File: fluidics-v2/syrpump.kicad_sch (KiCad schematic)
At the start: 7 parts, among them U5 MAX3221

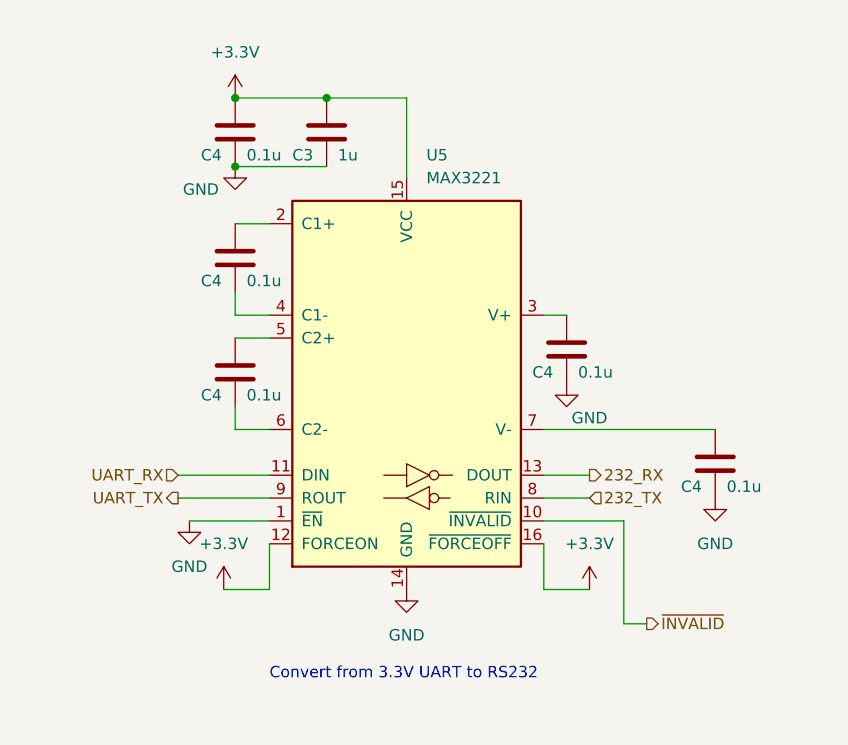
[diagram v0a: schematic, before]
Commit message: added footprints and mounting holes, cleaned up some sheets
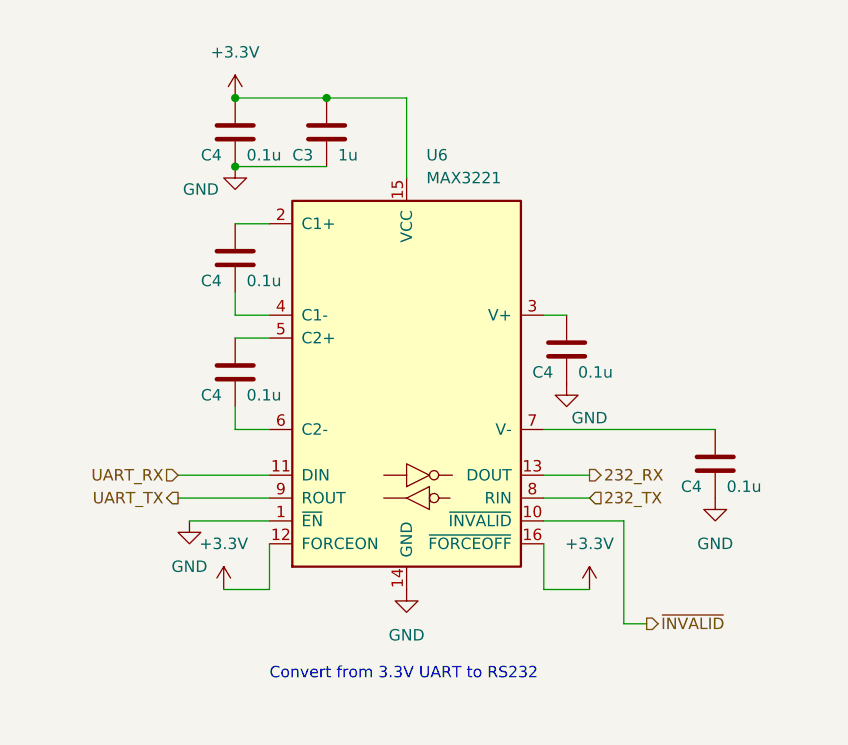
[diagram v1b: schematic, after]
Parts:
- renumbered U5 to U6
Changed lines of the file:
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@@
   (symbol (lib_id "power:+3.3V") (at 123.19 85.09 0) (unit 1)
     (in_bom yes) (on_board yes) (dnp no) (fields_autoplaced)
-    (property "Reference" "#PWR089" (at 123.19 88.9 0)
+    (property "Reference" "#PWR095" (at 123.19 88.9 0)
       (effects (font (size 1.27 1.27)) hide)
     )
@@
       (project "fluidics-v2"
         (path "/0ec91c42-8aad-437d-8c85-5e10f0e51fe0/40e657d1-9450-4917-aa0c-637ab5e93f67"
-          (reference "#PWR089") (unit 1)
+          (reference "#PWR095") (unit 1)
         )
       )
@@
   (symbol (lib_id "power:GND") (at 137.16 74.93 0) (unit 1)
     (in_bom yes) (on_board yes) (dnp no) (fields_autoplaced)
-    (property "Reference" "#PWR094" (at 137.16 81.28 0)
+    (property "Reference" "#PWR091" (at 137.16 81.28 0)
       (effects (font (size 1.27 1.27)) hide)
     )
@@
       (project "fluidics-v2"
         (path "/0ec91c42-8aad-437d-8c85-5e10f0e51fe0/40e657d1-9450-4917-aa0c-637ab5e93f67"
-          (reference "#PWR094") (unit 1)
+          (reference "#PWR091") (unit 1)
         )
       )
@@
         )
         (path "/0ec91c42-8aad-437d-8c85-5e10f0e51fe0/40e657d1-9450-4917-aa0c-637ab5e93f67"
-          (reference "C29") (unit 1)
+          (reference "C28") (unit 1)
         )
       )
@@
   (symbol (lib_id "power:GND") (at 83.82 38.1 0) (unit 1)
     (in_bom yes) (on_board yes) (dnp no)
-    (property "Reference" "#PWR092" (at 83.82 44.45 0)
+    (property "Reference" "#PWR089" (at 83.82 44.45 0)
       (effects (font (size 1.27 1.27)) hide)
     )
@@
       (project "fluidics-v2"
         (path "/0ec91c42-8aad-437d-8c85-5e10f0e51fe0/40e657d1-9450-4917-aa0c-637ab5e93f67"
-          (reference "#PWR092") (unit 1)
+          (reference "#PWR089") (unit 1)
         )
       )
@@
   (symbol (lib_id "power:+3.3V") (at 82.55 85.09 0) (unit 1)
     (in_bom yes) (on_board yes) (dnp no) (fields_autoplaced)
-    (property "Reference" "#PWR088" (at 82.55 88.9 0)
+    (property "Reference" "#PWR093" (at 82.55 88.9 0)
       (effects (font (size 1.27 1.27)) hide)
     )
@@
       (project "fluidics-v2"
         (path "/0ec91c42-8aad-437d-8c85-5e10f0e51fe0/40e657d1-9450-4917-aa0c-637ab5e93f67"
+          (reference "#PWR093") (unit 1)
+        )
+      )
+    )
+  )
+  (symbol (lib_id "power:GND") (at 120.65 62.23 0) (unit 1)
+    (in_bom yes) (on_board yes) (dnp no)
+    (property "Reference" "#PWR090" (at 120.65 68.58 0)
+      (effects (font (size 1.27 1.27)) hide)
+    )
+    (property "Value" "GND" (at 123.19 66.04 0)
+      (effects (font (size 1.27 1.27)))
+    )
+    (property "Footprint" "" (at 120.65 62.23 0)
+      (effects (font (size 1.27 1.27)) hide)
+    )
+    (property "Datasheet" "" (at 120.65 62.23 0)
+      (effects (font (size 1.27 1.27)) hide)
+    )
+    (pin "1")
+    (instances
+      (project "fluidics-v2"
+        (path "/0ec91c42-8aad-437d-8c85-5e10f0e51fe0/40e657d1-9450-4917-aa0c-637ab5e93f67"
+          (reference "#PWR090") (unit 1)
+        )
+      )
+    )
+  )
+  (symbol (lib_id "power:+3.3V") (at 83.82 30.48 0) (unit 1)
+    (in_bom yes) (on_board yes) (dnp no) (fields_autoplaced)
+    (property "Reference" "#PWR088" (at 83.82 34.29 0)
+      (effects (font (size 1.27 1.27)) hide)
+    )
+    (property "Value" "+3.3V" (at 83.82 25.4 0)
+      (effects (font (size 1.27 1.27)))
+    )
+    (property "Footprint" "" (at 83.82 30.48 0)
+      (effects (font (size 1.27 1.27)) hide)
+    )
+    (property "Datasheet" "" (at 83.82 30.48 0)
+      (effects (font (size 1.27 1.27)) hide)
+    )
+    (pin "1")
+    (instances
+      (project "fluidics-v2"
+        (path "/0ec91c42-8aad-437d-8c85-5e10f0e51fe0/40e657d1-9450-4917-aa0c-637ab5e93f67"
           (reference "#PWR088") (unit 1)
-        )
-      )
-    )
-  )
-  (symbol (lib_id "power:GND") (at 120.65 62.23 0) (unit 1)
-    (in_bom yes) (on_board yes) (dnp no)
-    (property "Reference" "#PWR093" (at 120.65 68.58 0)
-      (effects (font (size 1.27 1.27)) hide)
-    )
-    (property "Value" "GND" (at 123.19 66.04 0)
-      (effects (font (size 1.27 1.27)))
-    )
-    (property "Footprint" "" (at 120.65 62.23 0)
-      (effects (font (size 1.27 1.27)) hide)
-    )
-    (property "Datasheet" "" (at 120.65 62.23 0)
-      (effects (font (size 1.27 1.27)) hide)
-    )
-    (pin "1")
-    (instances
-      (project "fluidics-v2"
-        (path "/0ec91c42-8aad-437d-8c85-5e10f0e51fe0/40e657d1-9450-4917-aa0c-637ab5e93f67"
-          (reference "#PWR093") (unit 1)
-        )
-      )
-    )
-  )
-  (symbol (lib_id "power:+3.3V") (at 83.82 30.48 0) (unit 1)
-    (in_bom yes) (on_board yes) (dnp no) (fields_autoplaced)
-    (property "Reference" "#PWR087" (at 83.82 34.29 0)
-      (effects (font (size 1.27 1.27)) hide)
-    )
-    (property "Value" "+3.3V" (at 83.82 25.4 0)
-      (effects (font (size 1.27 1.27)))
-    )
-    (property "Footprint" "" (at 83.82 30.48 0)
-      (effects (font (size 1.27 1.27)) hide)
-    )
-    (property "Datasheet" "" (at 83.82 30.48 0)
-      (effects (font (size 1.27 1.27)) hide)
-    )
-    (pin "1")
-    (instances
-      (project "fluidics-v2"
-        (path "/0ec91c42-8aad-437d-8c85-5e10f0e51fe0/40e657d1-9450-4917-aa0c-637ab5e93f67"
-          (reference "#PWR087") (unit 1)
         )
       )
@@
   (symbol (lib_id "Interface_UART:MAX3221") (at 102.87 62.23 0) (unit 1)
     (in_bom yes) (on_board yes) (dnp no) (fields_autoplaced)
-    (property "Reference" "U5" (at 105.0641 36.83 0)
+    (property "Reference" "U6" (at 105.0641 36.83 0)
       (effects (font (size 1.27 1.27)) (justify left))
     )
@@
       (project "fluidics-v2"
         (path "/0ec91c42-8aad-437d-8c85-5e10f0e51fe0/40e657d1-9450-4917-aa0c-637ab5e93f67"
-          (reference "U5") (unit 1)
+          (reference "U6") (unit 1)
         )
       )
@@
         )
         (path "/0ec91c42-8aad-437d-8c85-5e10f0e51fe0/40e657d1-9450-4917-aa0c-637ab5e93f67"
-          (reference "C28") (unit 1)
+          (reference "C29") (unit 1)
         )
       )
@@
   (symbol (lib_id "power:GND") (at 78.74 77.47 0) (unit 1)
     (in_bom yes) (on_board yes) (dnp no) (fields_autoplaced)
-    (property "Reference" "#PWR091" (at 78.74 83.82 0)
+    (property "Reference" "#PWR092" (at 78.74 83.82 0)
       (effects (font (size 1.27 1.27)) hide)
     )
@@
       (project "fluidics-v2"
         (path "/0ec91c42-8aad-437d-8c85-5e10f0e51fe0/40e657d1-9450-4917-aa0c-637ab5e93f67"
-          (reference "#PWR091") (unit 1)
+          (reference "#PWR092") (unit 1)
         )
       )
@@
   (symbol (lib_id "power:GND") (at 102.87 85.09 0) (unit 1)
     (in_bom yes) (on_board yes) (dnp no) (fields_autoplaced)
-    (property "Reference" "#PWR090" (at 102.87 91.44 0)
+    (property "Reference" "#PWR094" (at 102.87 91.44 0)
       (effects (font (size 1.27 1.27)) hide)
     )
@@
       (project "fluidics-v2"
         (path "/0ec91c42-8aad-437d-8c85-5e10f0e51fe0/40e657d1-9450-4917-aa0c-637ab5e93f67"
-          (reference "#PWR090") (unit 1)
-        )
-      )
+          (reference "#PWR094") (unit 1)
+        )
+      )

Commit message: started layout
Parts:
- renumbered C4 to C?, C3 to C?, U6 to U9
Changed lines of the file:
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@@
   (symbol (lib_id "Device:C") (at 83.82 34.29 0) (unit 1)
     (in_bom yes) (on_board yes) (dnp no)
-    (property "Reference" "C4" (at 80.01 36.83 0)
+    (property "Reference" "C?" (at 80.01 36.83 0)
       (effects (font (size 1.27 1.27)) (justify left))
     )
@@
       (project "fluidics-v2"
         (path "/0ec91c42-8aad-437d-8c85-5e10f0e51fe0/c1c30de3-a3db-48df-8d6b-b2f91b9251f0"
-          (reference "C4") (unit 1)
-        )
-        (path "/0ec91c42-8aad-437d-8c85-5e10f0e51fe0/40e657d1-9450-4917-aa0c-637ab5e93f67"
-          (reference "C25") (unit 1)
+          (reference "C?") (unit 1)
+        )
+        (path "/0ec91c42-8aad-437d-8c85-5e10f0e51fe0/40e657d1-9450-4917-aa0c-637ab5e93f67"
+          (reference "C13") (unit 1)
         )
       )
@@
   (symbol (lib_id "power:+3.3V") (at 123.19 85.09 0) (unit 1)
     (in_bom yes) (on_board yes) (dnp no) (fields_autoplaced)
-    (property "Reference" "#PWR095" (at 123.19 88.9 0)
+    (property "Reference" "#PWR0122" (at 123.19 88.9 0)
       (effects (font (size 1.27 1.27)) hide)
     )
@@
       (project "fluidics-v2"
         (path "/0ec91c42-8aad-437d-8c85-5e10f0e51fe0/40e657d1-9450-4917-aa0c-637ab5e93f67"
-          (reference "#PWR095") (unit 1)
+          (reference "#PWR0122") (unit 1)
         )
       )
@@
   (symbol (lib_id "power:GND") (at 137.16 74.93 0) (unit 1)
     (in_bom yes) (on_board yes) (dnp no) (fields_autoplaced)
-    (property "Reference" "#PWR091" (at 137.16 81.28 0)
+    (property "Reference" "#PWR0123" (at 137.16 81.28 0)
       (effects (font (size 1.27 1.27)) hide)
     )
@@
       (project "fluidics-v2"
         (path "/0ec91c42-8aad-437d-8c85-5e10f0e51fe0/40e657d1-9450-4917-aa0c-637ab5e93f67"
-          (reference "#PWR091") (unit 1)
+          (reference "#PWR0123") (unit 1)
         )
       )
@@
   (symbol (lib_id "Device:C") (at 120.65 58.42 0) (unit 1)
     (in_bom yes) (on_board yes) (dnp no)
-    (property "Reference" "C4" (at 116.84 60.96 0)
+    (property "Reference" "C?" (at 116.84 60.96 0)
       (effects (font (size 1.27 1.27)) (justify left))
     )
@@
       (project "fluidics-v2"
         (path "/0ec91c42-8aad-437d-8c85-5e10f0e51fe0/c1c30de3-a3db-48df-8d6b-b2f91b9251f0"
-          (reference "C4") (unit 1)
-        )
-        (path "/0ec91c42-8aad-437d-8c85-5e10f0e51fe0/40e657d1-9450-4917-aa0c-637ab5e93f67"
-          (reference "C28") (unit 1)
+          (reference "C?") (unit 1)
+        )
+        (path "/0ec91c42-8aad-437d-8c85-5e10f0e51fe0/40e657d1-9450-4917-aa0c-637ab5e93f67"
+          (reference "C17") (unit 1)
         )
       )
@@
   (symbol (lib_id "Device:C") (at 93.98 34.29 0) (unit 1)
     (in_bom yes) (on_board yes) (dnp no)
-    (property "Reference" "C3" (at 90.17 36.83 0)
+    (property "Reference" "C?" (at 90.17 36.83 0)
       (effects (font (size 1.27 1.27)) (justify left))
     )
@@
       (project "fluidics-v2"
         (path "/0ec91c42-8aad-437d-8c85-5e10f0e51fe0/c1c30de3-a3db-48df-8d6b-b2f91b9251f0"
-          (reference "C3") (unit 1)
-        )
-        (path "/0ec91c42-8aad-437d-8c85-5e10f0e51fe0/40e657d1-9450-4917-aa0c-637ab5e93f67"
-          (reference "C26") (unit 1)
+          (reference "C?") (unit 1)
+        )
+        (path "/0ec91c42-8aad-437d-8c85-5e10f0e51fe0/40e657d1-9450-4917-aa0c-637ab5e93f67"
+          (reference "C16") (unit 1)
         )
       )
@@
   (symbol (lib_id "power:GND") (at 83.82 38.1 0) (unit 1)
     (in_bom yes) (on_board yes) (dnp no)
-    (property "Reference" "#PWR089" (at 83.82 44.45 0)
+    (property "Reference" "#PWR0119" (at 83.82 44.45 0)
       (effects (font (size 1.27 1.27)) hide)
     )
@@
       (project "fluidics-v2"
         (path "/0ec91c42-8aad-437d-8c85-5e10f0e51fe0/40e657d1-9450-4917-aa0c-637ab5e93f67"
-          (reference "#PWR089") (unit 1)
+          (reference "#PWR0119") (unit 1)
         )
       )
@@
   (symbol (lib_id "Device:C") (at 83.82 48.26 0) (unit 1)
     (in_bom yes) (on_board yes) (dnp no)
-    (property "Reference" "C4" (at 80.01 50.8 0)
+    (property "Reference" "C?" (at 80.01 50.8 0)
       (effects (font (size 1.27 1.27)) (justify left))
     )
@@
       (project "fluidics-v2"
         (path "/0ec91c42-8aad-437d-8c85-5e10f0e51fe0/c1c30de3-a3db-48df-8d6b-b2f91b9251f0"
-          (reference "C4") (unit 1)
-        )
-        (path "/0ec91c42-8aad-437d-8c85-5e10f0e51fe0/40e657d1-9450-4917-aa0c-637ab5e93f67"
-          (reference "C27") (unit 1)
+          (reference "C?") (unit 1)
+        )
+        (path "/0ec91c42-8aad-437d-8c85-5e10f0e51fe0/40e657d1-9450-4917-aa0c-637ab5e93f67"
+          (reference "C14") (unit 1)
         )
       )
@@
   (symbol (lib_id "power:+3.3V") (at 82.55 85.09 0) (unit 1)
     (in_bom yes) (on_board yes) (dnp no) (fields_autoplaced)
-    (property "Reference" "#PWR093" (at 82.55 88.9 0)
+    (property "Reference" "#PWR0117" (at 82.55 88.9 0)
       (effects (font (size 1.27 1.27)) hide)
     )
@@
       (project "fluidics-v2"
         (path "/0ec91c42-8aad-437d-8c85-5e10f0e51fe0/40e657d1-9450-4917-aa0c-637ab5e93f67"
-          (reference "#PWR093") (unit 1)
+          (reference "#PWR0117") (unit 1)
         )
       )
@@
   (symbol (lib_id "power:GND") (at 120.65 62.23 0) (unit 1)
     (in_bom yes) (on_board yes) (dnp no)
-    (property "Reference" "#PWR090" (at 120.65 68.58 0)
+    (property "Reference" "#PWR0121" (at 120.65 68.58 0)
       (effects (font (size 1.27 1.27)) hide)
     )
@@
       (project "fluidics-v2"
         (path "/0ec91c42-8aad-437d-8c85-5e10f0e51fe0/40e657d1-9450-4917-aa0c-637ab5e93f67"
-          (reference "#PWR090") (unit 1)
+          (reference "#PWR0121") (unit 1)
         )
       )
@@
   (symbol (lib_id "power:+3.3V") (at 83.82 30.48 0) (unit 1)
     (in_bom yes) (on_board yes) (dnp no) (fields_autoplaced)
-    (property "Reference" "#PWR088" (at 83.82 34.29 0)
+    (property "Reference" "#PWR0118" (at 83.82 34.29 0)
       (effects (font (size 1.27 1.27)) hide)
     )
@@
       (project "fluidics-v2"
         (path "/0ec91c42-8aad-437d-8c85-5e10f0e51fe0/40e657d1-9450-4917-aa0c-637ab5e93f67"
-          (reference "#PWR088") (unit 1)
+          (reference "#PWR0118") (unit 1)
         )
       )
@@
   (symbol (lib_id "Device:C") (at 137.16 71.12 0) (unit 1)
     (in_bom yes) (on_board yes) (dnp no)
-    (property "Reference" "C4" (at 133.35 73.66 0)
+    (property "Reference" "C?" (at 133.35 73.66 0)
       (effects (font (size 1.27 1.27)) (justify left))
     )
@@
       (project "fluidics-v2"
         (path "/0ec91c42-8aad-437d-8c85-5e10f0e51fe0/c1c30de3-a3db-48df-8d6b-b2f91b9251f0"
-          (reference "C4") (unit 1)
-        )
-        (path "/0ec91c42-8aad-437d-8c85-5e10f0e51fe0/40e657d1-9450-4917-aa0c-637ab5e93f67"
-          (reference "C30") (unit 1)
+          (reference "C?") (unit 1)
+        )
+        (path "/0ec91c42-8aad-437d-8c85-5e10f0e51fe0/40e657d1-9450-4917-aa0c-637ab5e93f67"
+          (reference "C18") (unit 1)
         )
       )
@@
   (symbol (lib_id "Interface_UART:MAX3221") (at 102.87 62.23 0) (unit 1)
     (in_bom yes) (on_board yes) (dnp no) (fields_autoplaced)
-    (property "Reference" "U6" (at 105.0641 36.83 0)
+    (property "Reference" "U9" (at 105.0641 36.83 0)
       (effects (font (size 1.27 1.27)) (justify left))
     )
@@
       (project "fluidics-v2"
         (path "/0ec91c42-8aad-437d-8c85-5e10f0e51fe0/40e657d1-9450-4917-aa0c-637ab5e93f67"
-          (reference "U6") (unit 1)
+          (reference "U9") (unit 1)
         )
       )
@@
   (symbol (lib_id "Device:C") (at 83.82 60.96 0) (unit 1)
     (in_bom yes) (on_board yes) (dnp no)
-    (property "Reference" "C4" (at 80.01 63.5 0)
+    (property "Reference" "C?" (at 80.01 63.5 0)
       (effects (font (size 1.27 1.27)) (justify left))
     )
@@
       (project "fluidics-v2"
         (path "/0ec91c42-8aad-437d-8c85-5e10f0e51fe0/c1c30de3-a3db-48df-8d6b-b2f91b9251f0"
-          (reference "C4") (unit 1)
-        )
-        (path "/0ec91c42-8aad-437d-8c85-5e10f0e51fe0/40e657d1-9450-4917-aa0c-637ab5e93f67"
-          (reference "C29") (unit 1)
+          (reference "C?") (unit 1)
+        )
+        (path "/0ec91c42-8aad-437d-8c85-5e10f0e51fe0/40e657d1-9450-4917-aa0c-637ab5e93f67"
+          (reference "C15") (unit 1)
         )
       )
@@
   (symbol (lib_id "power:GND") (at 78.74 77.47 0) (unit 1)
     (in_bom yes) (on_board yes) (dnp no) (fields_autoplaced)
-    (property "Reference" "#PWR092" (at 78.74 83.82 0)
+    (property "Reference" "#PWR0116" (at 78.74 83.82 0)
       (effects (font (size 1.27 1.27)) hide)
     )
@@
       (project "fluidics-v2"
         (path "/0ec91c42-8aad-437d-8c85-5e10f0e51fe0/40e657d1-9450-4917-aa0c-637ab5e93f67"
-          (reference "#PWR092") (unit 1)
+          (reference "#PWR0116") (unit 1)
         )
       )
@@
   (symbol (lib_id "power:GND") (at 102.87 85.09 0) (unit 1)
     (in_bom yes) (on_board yes) (dnp no) (fields_autoplaced)
-    (property "Reference" "#PWR094" (at 102.87 91.44 0)
+    (property "Reference" "#PWR0120" (at 102.87 91.44 0)
       (effects (font (size 1.27 1.27)) hide)
     )
@@
       (project "fluidics-v2"
         (path "/0ec91c42-8aad-437d-8c85-5e10f0e51fe0/40e657d1-9450-4917-aa0c-637ab5e93f67"
-          (reference "#PWR094") (unit 1)
-        )
-      )
+          (reference "#PWR0120") (unit 1)
+        )
+      )

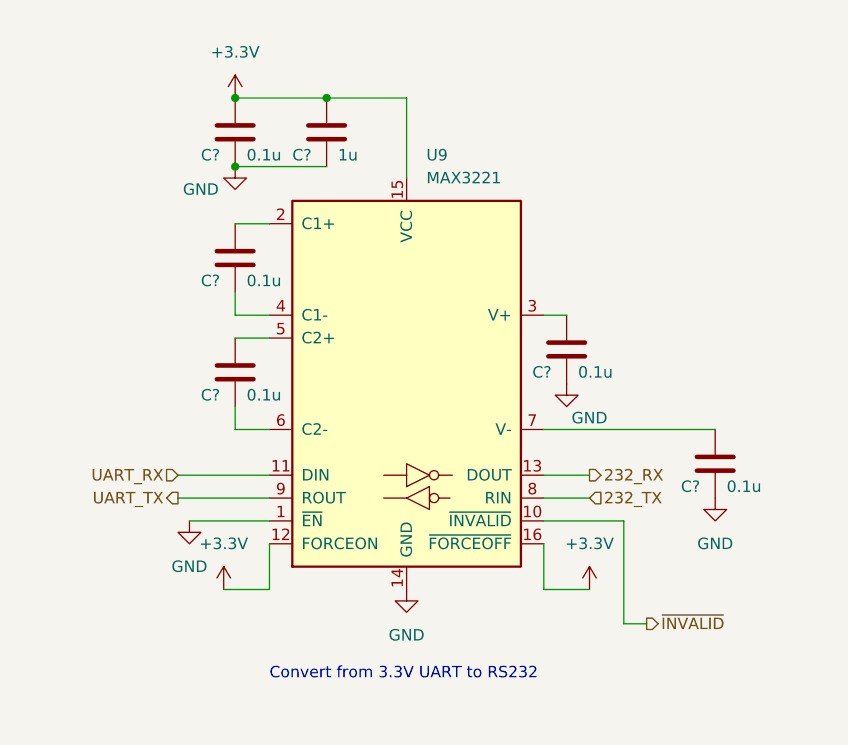
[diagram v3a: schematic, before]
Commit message: added pressure controllers and more flow sensors
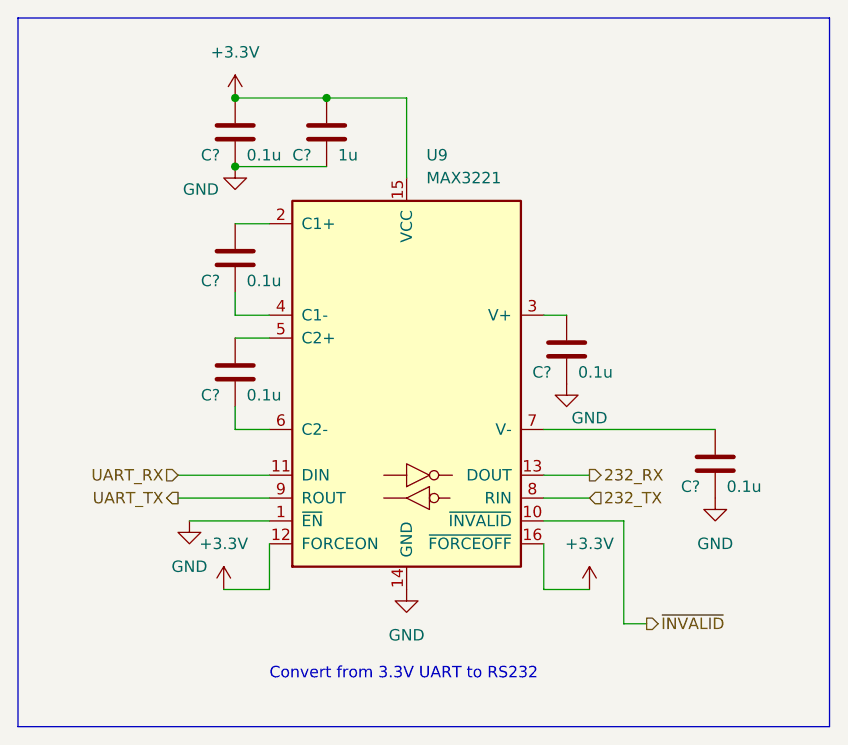
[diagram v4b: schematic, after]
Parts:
- C?: footprint Capacitor_SMD:C_0603_1608Metric -> Capacitor_SMD:C_0805_2012Metric
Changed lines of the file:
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@@
     (stroke (width 0) (type default))
+  )
+  (rectangle (start 59.69 21.59) (end 149.86 100.33)
+    (stroke (width 0) (type default))
+    (fill (type none))
   )
   (text "Convert from 3.3V UART to RS232" (at 87.63 95.25 0)
@@
       (effects (font (size 1.27 1.27)) (justify left))
     )
-    (property "Footprint" "Capacitor_SMD:C_0603_1608Metric" (at 94.9452 38.1 0)
+    (property "Footprint" "Capacitor_SMD:C_0805_2012Metric" (at 94.9452 38.1 0)
       (effects (font (size 1.27 1.27)) hide)
     )
